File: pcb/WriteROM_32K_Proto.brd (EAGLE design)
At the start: 22.9 x 81.3 mm, 18 parts, among them IC1 23256-RP, IC2 XC9572XLTQG100, IC5 SST39SF040APHR

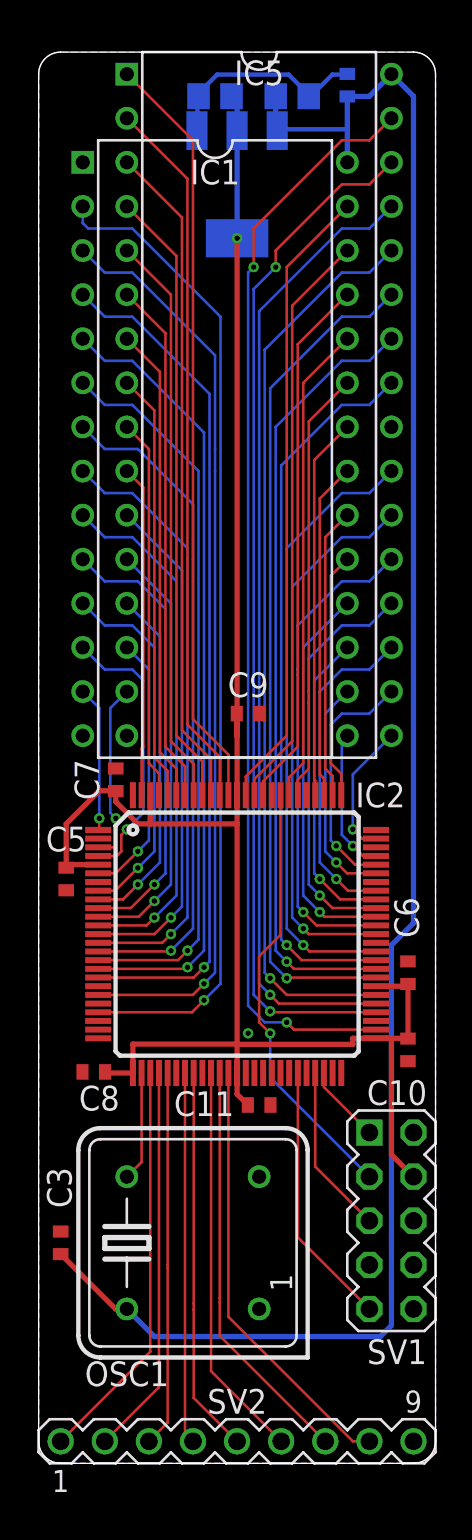
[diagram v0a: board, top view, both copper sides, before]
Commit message: Added more flexibility to banking
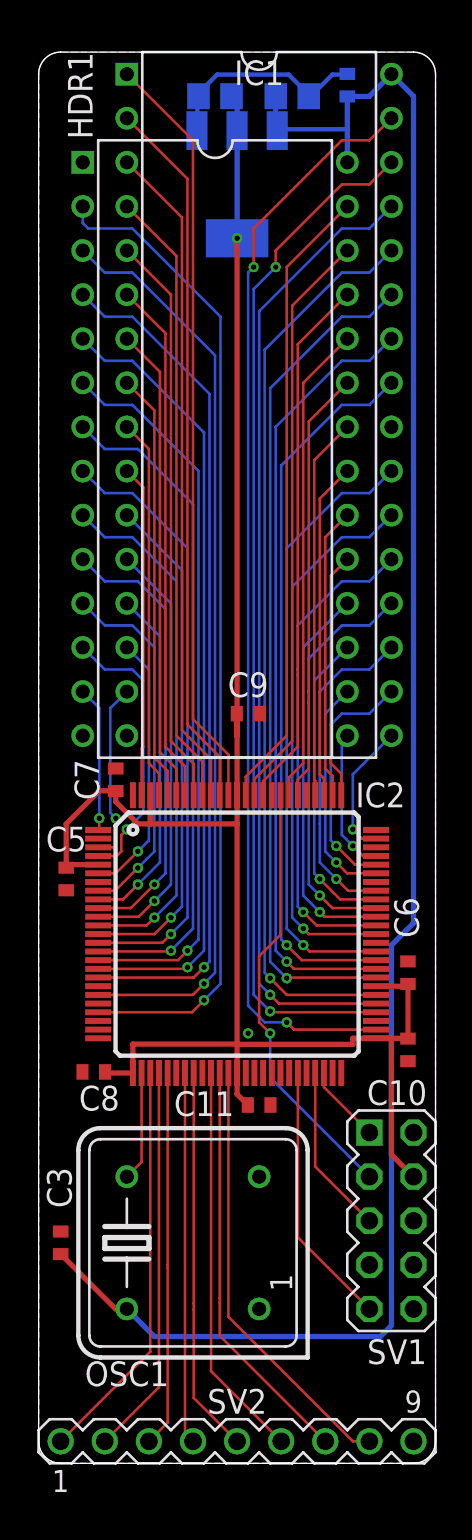
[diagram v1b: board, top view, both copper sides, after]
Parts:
- removed IC5: SST39SF040APHR, memory-sst:DIL32-RP
- added HDR1: (no value), memory-rp:DIL28
- IC1: value 23256-RP -> SST39SF040APHR; device commodore:DIL28-ROUNDPAD -> memory-sst:DIL32-RP
- moved IC1 3.59 mm to (1.27, 40.6)
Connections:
- net N$1 renamed SIZE0
- net N$2 renamed SIZE1
- removed net $2: IC2.23
- new net !FOE: IC1.24, IC2.25
- new net A15: HDR1.1, IC2.23
- net !CE: now also HDR1.20; no longer IC1.20
- net !FCE: now also IC1.22; no longer IC5.22
- net !FWE: now also IC1.31; no longer IC5.31
- net !OE: now also HDR1.22; no longer IC1.22
- net +5V: now also HDR1.28, IC1.32; no longer IC1.28, IC5.32
- net A0: now also HDR1.10; no longer IC1.10
- net A1: now also HDR1.9; no longer IC1.9
- net A10: now also HDR1.21; no longer IC1.21
- net A11: now also HDR1.23; no longer IC1.23
- net A12: now also HDR1.2; no longer IC1.2
- net A13: now also HDR1.26; no longer IC1.26
- net A14: now also HDR1.27; no longer IC1.27
- net A2: now also HDR1.8; no longer IC1.8
- net A3: now also HDR1.7; no longer IC1.7
- net A4: now also HDR1.6; no longer IC1.6
- net A5: now also HDR1.5; no longer IC1.5
- net A6: now also HDR1.4; no longer IC1.4
- net A7: now also HDR1.3; no longer IC1.3
- net A8: now also HDR1.25; no longer IC1.25
- net A9: now also HDR1.24; no longer IC1.24
- net BA0: now also IC1.12; no longer IC5.12
- net BA1: now also IC1.11; no longer IC5.11
- net BA10: now also IC1.23; no longer IC5.23
- net BA11: now also IC1.25; no longer IC5.25
- net BA12: now also IC1.4; no longer IC5.4
- net BA13: now also IC1.28; no longer IC5.28
- net BA14: now also IC1.29; no longer IC5.29
- net BA15: now also IC1.3; no longer IC5.3
- net BA16: now also IC1.2; no longer IC5.2
- net BA17: now also IC1.30; no longer IC5.30
- net BA18: now also IC1.1; no longer IC5.1
- net BA2: now also IC1.10; no longer IC5.10
- net BA3: now also IC1.9; no longer IC5.9
- net BA4: now also IC1.8; no longer IC5.8
- net BA5: now also IC1.7; no longer IC5.7
- net BA6: now also IC1.6; no longer IC5.6
- net BA7: now also IC1.5; no longer IC5.5
- net BA8: now also IC1.27; no longer IC5.27
- net BA9: now also IC1.26; no longer IC5.26
- net BD0: now also IC1.13; no longer IC5.13
- net BD1: now also IC1.14; no longer IC5.14
- net BD2: now also IC1.15; no longer IC5.15
- net BD3: now also IC1.17; no longer IC5.17
- net BD4: now also IC1.18; no longer IC5.18
- net BD5: now also IC1.19; no longer IC5.19
- net BD6: now also IC1.20; no longer IC5.20
- net BD7: now also IC1.21; no longer IC5.21
- net D0: now also HDR1.11; no longer IC1.11
- net D1: now also HDR1.12; no longer IC1.12
- net D2: now also HDR1.13; no longer IC1.13
- net D3: now also HDR1.15; no longer IC1.15
- net D4: now also HDR1.16; no longer IC1.16
- net D5: now also HDR1.17; no longer IC1.17
- net D6: now also HDR1.18; no longer IC1.18
- net D7: now also HDR1.19; no longer IC1.19
- net GND: now also HDR1.14, IC1.16; no longer IC1.14, IC5.16, IC5.24
